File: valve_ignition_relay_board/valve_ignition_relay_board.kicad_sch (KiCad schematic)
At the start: 24 parts, among them J1 Programming Header, J5 CAN Connector Left, J6 CAN Connector Right, U1 PIC18F26K83, U2 MCP2562, Y1 12 MHz

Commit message: Valve Ignition Relay - ready for review 1
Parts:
- F2: value Fuse -> 150mA; footprint (none) -> Fuse:Fuse_1206_3216Metric_Pad1.42x1.75mm_HandSolder
- F3: value 200A -> 200mA; footprint (none) -> Fuse:Fuse_1206_3216Metric_Pad1.42x1.75mm_HandSolder
- TP1, TP2, TP3: footprint (none) -> TestPoint:TestPoint_Keystone_5000-5004_Miniature
- U1: footprint (none) -> Package_SO:SOIC-28W_7.5x18.7mm_P1.27mm
- U2: footprint (none) -> Package_SO:SOIC-8_3.9x4.9mm_P1.27mm
- Y1: footprint (none) -> Crystal:Crystal_HC49-4H_Vertical
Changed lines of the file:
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@@
 			)
 		)
-		(property "Footprint" ""
+		(property "Footprint" "Crystal:Crystal_HC49-4H_Vertical"
 			(at 139.7 149.86 0)
 			(effects
@@
 			)
 		)
-		(property "Value" "Fuse"
-			(at 60.96 37.846 0)
+		(property "Value" "150mA"
+			(at 58.674 37.846 0)
 			(effects
 				(font
@@
 			)
 		)
-		(property "Footprint" ""
+		(property "Footprint" "Fuse:Fuse_1206_3216Metric_Pad1.42x1.75mm_HandSolder"
 			(at 65.532 36.83 90)
 			(effects
@@
 			)
 		)
-		(property "Footprint" ""
+		(property "Footprint" "Package_SO:SOIC-8_3.9x4.9mm_P1.27mm"
 			(at 254 138.43 0)
 			(effects
@@
 			)
 		)
-		(property "Footprint" ""
+		(property "Footprint" "TestPoint:TestPoint_Keystone_5000-5004_Miniature"
 			(at 248.92 25.4 0)
 			(effects
@@
 			)
 		)
-		(property "Footprint" ""
+		(property "Footprint" "TestPoint:TestPoint_Keystone_5000-5004_Miniature"
 			(at 246.38 24.13 0)
 			(effects
@@
 			)
 		)
-		(property "Value" "200A"
+		(property "Value" "200mA"
 			(at 77.47 38.0999 0)
 			(effects
@@
 			)
 		)
-		(property "Footprint" ""
+		(property "Footprint" "Fuse:Fuse_1206_3216Metric_Pad1.42x1.75mm_HandSolder"
 			(at 73.152 36.83 90)
 			(effects
@@
 			)
 		)
-		(property "Footprint" ""
+		(property "Footprint" "Package_SO:SOIC-28W_7.5x18.7mm_P1.27mm"
 			(at 181.61 81.28 0)
 			(effects
@@
 			)
 		)
-		(property "Footprint" ""
+		(property "Footprint" "TestPoint:TestPoint_Keystone_5000-5004_Miniature"
 			(at 262.89 25.4 0)
 			(effects

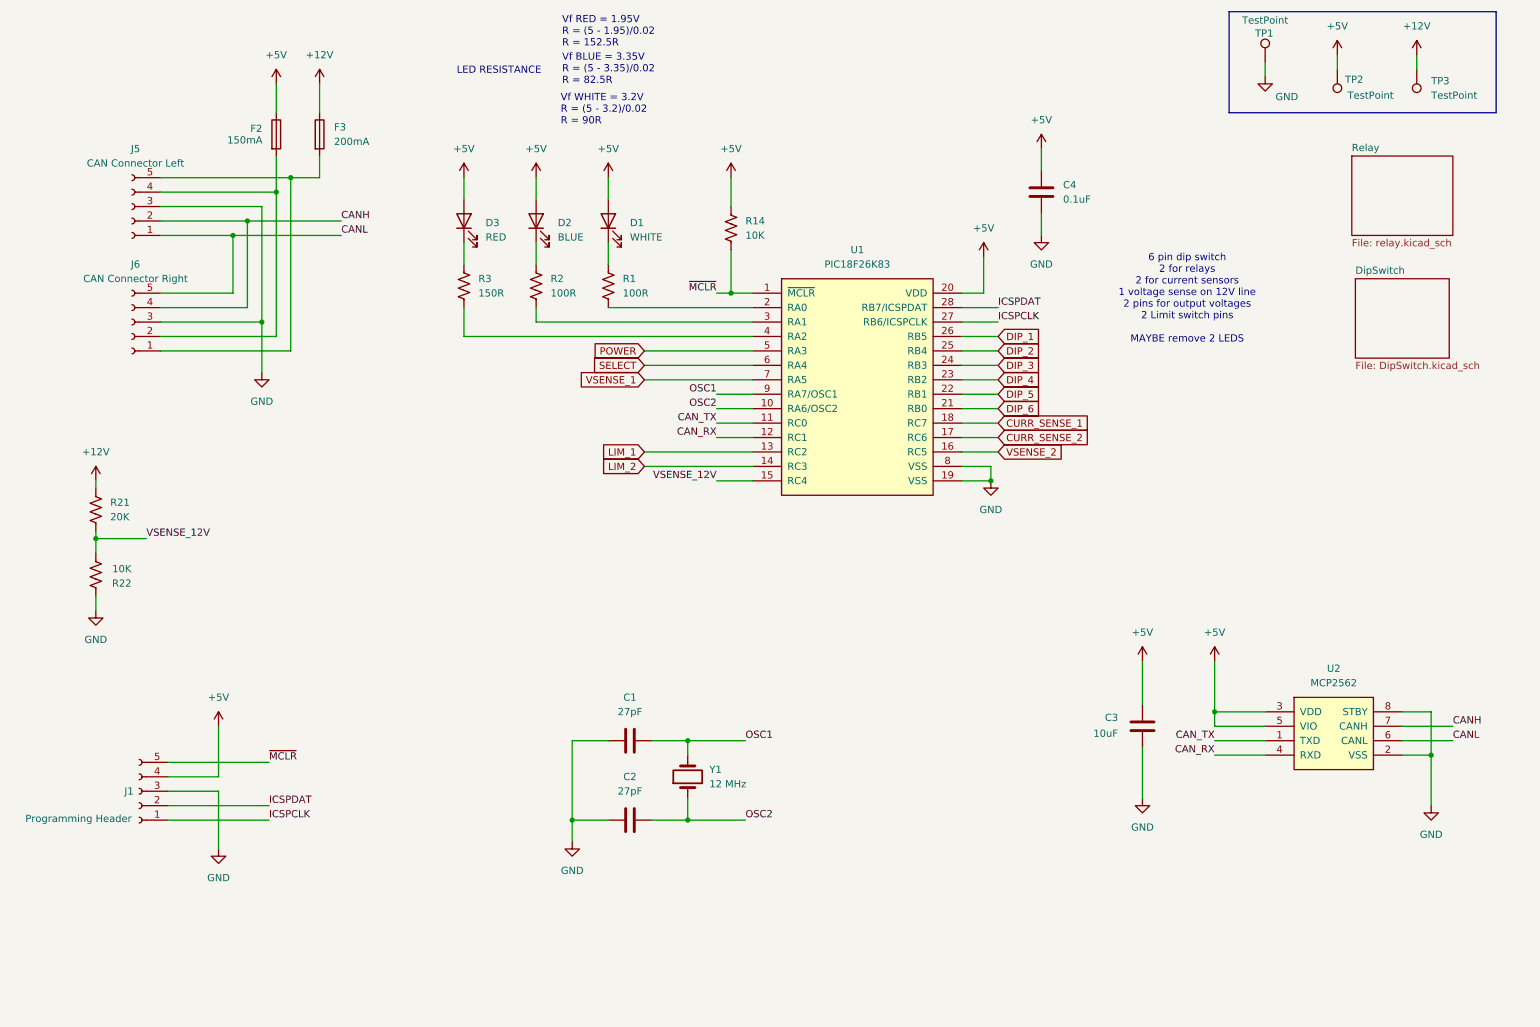
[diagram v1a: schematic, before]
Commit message: Added IO Expander and moved dip switch
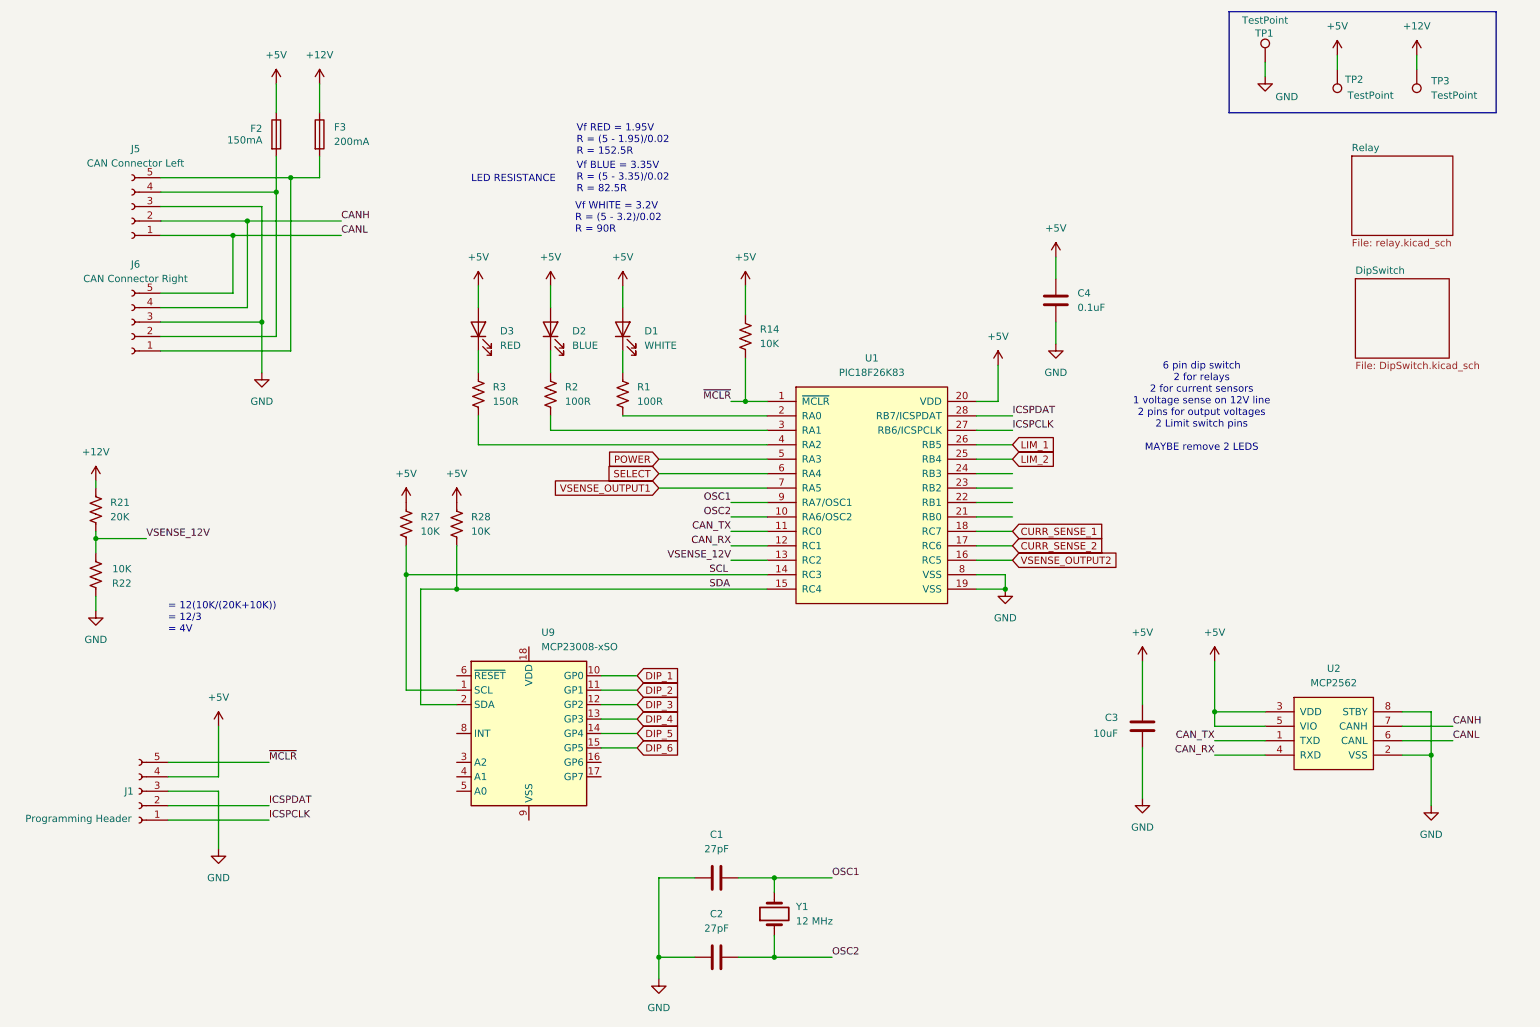
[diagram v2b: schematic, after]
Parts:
- added R27, R28: 10K, Resistor_SMD:R_0805_2012Metric_Pad1.20x1.40mm_HandSolder, symbol Device:R_US
- added U9: MCP23008-xSO, Package_SO:SOIC-18W_7.5x11.6mm_P1.27mm, symbol Interface_Expansion:MCP23008-xSO
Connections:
- net +5V: now also R27.1, R28.1
- net DIP_1: now also U9.10 (GP0); no longer U1.26 (RB5)
- net DIP_2: now also U9.11 (GP1); no longer U1.25 (RB4)
- net DIP_3: now also U9.12 (GP2); no longer U1.24 (RB3)
- net DIP_4: now also U9.13 (GP3); no longer U1.23 (RB2)
- net DIP_5: now also U9.14 (GP4); no longer U1.22 (RB1)
- net DIP_6: now also U9.15 (GP5); no longer U1.21 (RB0)
- net LIM_1: now also U1.26 (RB5); no longer U1.13 (RC2)
- net LIM_2: now also U1.25 (RB4); no longer U1.14 (RC3)
- net VSENSE_12V: now also U1.13 (RC2); no longer U1.15 (RC4)
- net VSENSE_1 renamed VSENSE_OUTPUT1
- net VSENSE_2 renamed VSENSE_OUTPUT2
- new net SCL: R27.2, U1.14 (RC3), U9.1 (SCL)
- new net SDA: R28.2, U1.15 (RC4), U9.2 (SDA)
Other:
- note added: "= 12(10K/(20K+10K)) = 12/3 = 4V"
- moved on the sheet: C1, C2, C4, D1, D2, D3, R1, R14, R2, R3, U1, Y1
